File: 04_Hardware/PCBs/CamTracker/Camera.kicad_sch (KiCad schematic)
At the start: 35 parts, among them J10 1.25x15P, J11 22-28-4034, J12 22-28-4034, J9 1.25x15P, U1 SC206EEMDA-G51-UGNDA

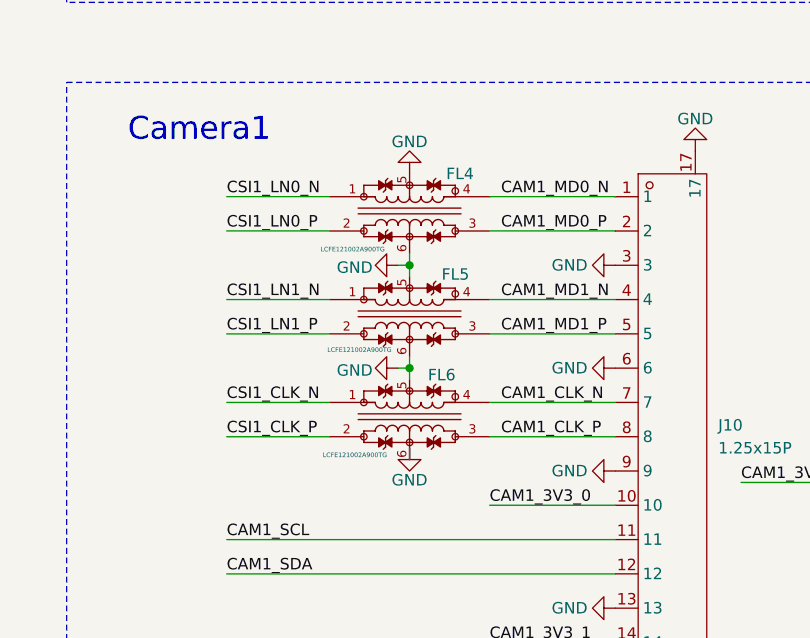
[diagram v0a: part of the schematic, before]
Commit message: feat: Completed Placement v1 in Layout
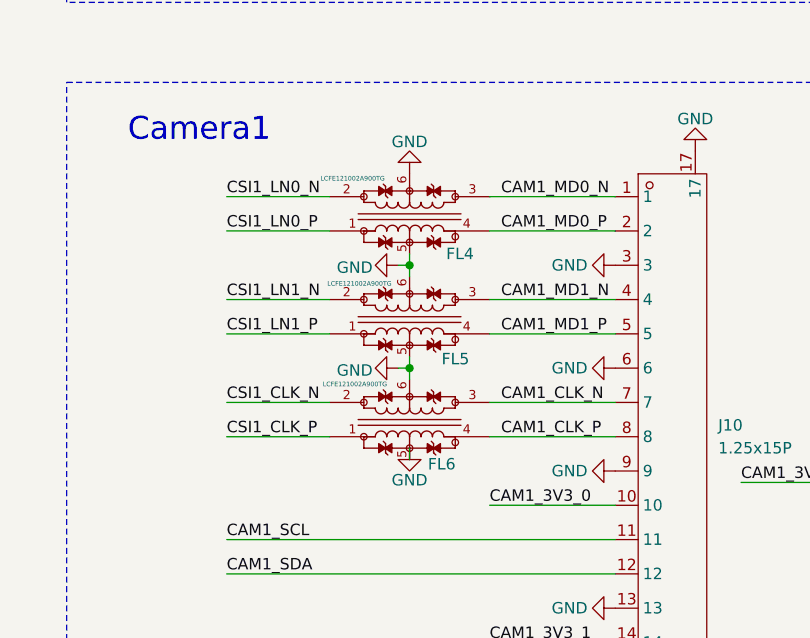
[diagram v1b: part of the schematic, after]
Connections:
- net CAM1_CLK_N: now also FL6.3; no longer FL6.4
- net CAM1_CLK_P: now also FL6.4; no longer FL6.3
- net CAM1_MD0_N: now also FL4.3; no longer FL4.4
- net CAM1_MD0_P: now also FL4.4; no longer FL4.3
- net CAM1_MD1_N: now also FL5.3; no longer FL5.4
- net CAM1_MD1_P: now also FL5.4; no longer FL5.3
- net CSI1_CLK_N: now also FL6.2; no longer FL6.1
- net CSI1_CLK_P: now also FL6.1; no longer FL6.2
- net CSI1_LN0_N: now also FL4.2; no longer FL4.1
- net CSI1_LN0_P: now also FL4.1; no longer FL4.2
- net CSI1_LN1_N: now also FL5.2; no longer FL5.1
- net CSI1_LN1_P: now also FL5.1; no longer FL5.2
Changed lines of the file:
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@@
 	(wire
 		(pts
+			(xy 195.58 152.4) (xy 195.58 151.13)
+		)
+		(stroke
+			(width 0)
+			(type default)
+		)
+	)
+	(wire
+		(pts
 			(xy 195.58 162.56) (xy 194.31 162.56)
 		)
@@
 	(wire
 		(pts
-			(xy 195.58 171.45) (xy 195.58 172.72)
+			(xy 195.58 161.29) (xy 195.58 162.56)
 		)
 		(stroke
@@
 	(wire
 		(pts
-			(xy 175.26 67.31) (xy 186.69 67.31)
+			(xy 195.58 171.45) (xy 195.58 172.72)
 		)
 		(stroke
@@
 	(wire
 		(pts
-			(xy 100.33 118.11) (xy 81.28 118.11)
+			(xy 175.26 67.31) (xy 186.69 67.31)
 		)
 		(stroke
@@
 	(wire
 		(pts
-			(xy 175.26 52.07) (xy 186.69 52.07)
+			(xy 100.33 118.11) (xy 81.28 118.11)
 		)
 		(stroke
@@
 	(wire
 		(pts
-			(xy 274.32 72.39) (xy 274.32 71.12)
+			(xy 175.26 52.07) (xy 186.69 52.07)
 		)
 		(stroke
@@
 	(wire
 		(pts
-			(xy 294.64 175.26) (xy 290.83 175.26)
+			(xy 274.32 72.39) (xy 274.32 71.12)
 		)
 		(stroke
@@
 	(wire
 		(pts
-			(xy 195.58 151.13) (xy 195.58 152.4)
+			(xy 294.64 175.26) (xy 290.83 175.26)
 		)
 		(stroke
@@
 	(wire
 		(pts
+			(xy 195.58 58.42) (xy 195.58 59.69)
+		)
+		(stroke
+			(width 0)
+			(type default)
+		)
+	)
+	(wire
+		(pts
 			(xy 252.73 212.09) (xy 252.73 210.82)
 		)
@@
 	(wire
 		(pts
-			(xy 195.58 149.86) (xy 195.58 151.13)
-		)
-		(stroke
-			(width 0)
-			(type default)
-		)
-	)
-	(wire
-		(pts
 			(xy 201.93 214.63) (xy 213.36 214.63)
 		)
@@
 	(wire
 		(pts
-			(xy 270.51 72.39) (xy 274.32 72.39)
+			(xy 195.58 149.86) (xy 195.58 151.13)
 		)
 		(stroke
@@
 	(wire
 		(pts
-			(xy 175.26 166.37) (xy 186.69 166.37)
+			(xy 270.51 72.39) (xy 274.32 72.39)
 		)
 		(stroke
@@
 	(wire
 		(pts
-			(xy 100.33 76.2) (xy 81.28 76.2)
+			(xy 175.26 166.37) (xy 186.69 166.37)
 		)
 		(stroke
@@
 	(wire
 		(pts
-			(xy 81.28 185.42) (xy 100.33 185.42)
+			(xy 100.33 76.2) (xy 81.28 76.2)
 		)
 		(stroke
@@
 	(wire
 		(pts
-			(xy 195.58 151.13) (xy 194.31 151.13)
+			(xy 81.28 185.42) (xy 100.33 185.42)
 		)
 		(stroke
@@
 	(wire
 		(pts
-			(xy 100.33 106.68) (xy 81.28 106.68)
+			(xy 195.58 151.13) (xy 194.31 151.13)
 		)
 		(stroke
@@
 	(wire
 		(pts
-			(xy 195.58 161.29) (xy 195.58 162.56)
+			(xy 100.33 106.68) (xy 81.28 106.68)
 		)
 		(stroke
@@
 	(wire
 		(pts
-			(xy 195.58 60.96) (xy 195.58 59.69)
-		)
-		(stroke
-			(width 0)
-			(type default)
-		)
-	)
-	(wire
-		(pts
 			(xy 81.28 189.23) (xy 100.33 189.23)
 		)
@@
 	(wire
 		(pts
-			(xy 195.58 58.42) (xy 195.58 59.69)
-		)
-		(stroke
-			(width 0)
-			(type default)
-		)
-	)
-	(wire
-		(pts
 			(xy 292.1 162.56) (xy 276.86 162.56)
 		)
@@
 	(wire
 		(pts
+			(xy 195.58 60.96) (xy 195.58 59.69)
+		)
+		(stroke
+			(width 0)
+			(type default)
+		)
+	)
+	(wire
+		(pts
 			(xy 195.58 163.83) (xy 195.58 162.56)
 		)
@@
 	(symbol
 		(lib_id "000MCLib:LCFE121002A900TG")
-		(at 195.58 146.05 0)
-		(mirror x)
+		(at 195.58 144.78 0)
 		(unit 1)
 		(exclude_from_sim no)
@@
 		(dnp no)
 		(property "Reference" "FL4"
-			(at 199.644 140.97 0)
+			(at 199.644 149.86 0)
 			(effects
 				(font
@@
 		)
 		(property "Value" "LCFE121002A900TG"
-			(at 185.674 149.352 0)
+			(at 185.674 141.478 0)
 			(effects
 				(font
@@
 		)
 		(property "Footprint" "000MCLib:LCFE121002A900TG"
-			(at 222.25 68.91 0)
+			(at 222.25 221.92 0)
 			(effects
 				(font
@@
 		)
 		(property "Datasheet" "https://www.littelfuse.com/~/media/electronics/datasheets/emc_components/littelfuse_emi_filter_lcfe_datasheet.pdf.pdf"
-			(at 222.25 -31.09 0)
+			(at 222.25 321.92 0)
 			(effects
 				(font
@@
 		)
 		(property "Description" "Common Mode Chokes / Filters 90ohms 25% 100A 2 Lines 1210"
-			(at 195.58 144.78 0)
+			(at 195.58 146.05 0)
 			(effects
 				(font
@@
 		)
 		(property "Manufacturer" "LITTELFUSE"
-			(at 222.25 -531.09 0)
+			(at 222.25 821.92 0)
 			(effects
 				(font
@@
 		)
 		(property "Part Number" "LCFE121002A900TG"
-			(at 222.25 -631.09 0)
+			(at 222.25 921.92 0)
 			(effects
 				(font
@@
 	(symbol
 		(lib_id "000MCLib:LCFE121002A900TG")
-		(at 195.58 157.48 0)
-		(mirror x)
+		(at 195.58 156.21 0)
 		(unit 1)
 		(exclude_from_sim no)
@@
 		(dnp no)
 		(property "Reference" "FL5"
-			(at 199.136 152.146 0)
+			(at 199.136 161.544 0)
 			(effects
 				(font
@@
 		)
 		(property "Value" "LCFE121002A900TG"
-			(at 186.436 160.528 0)
+			(at 186.436 153.162 0)
 			(effects
 				(font
@@
 		)
 		(property "Footprint" "000MCLib:LCFE121002A900TG"
-			(at 222.25 80.34 0)
+			(at 222.25 233.35 0)
 			(effects
 				(font
@@
 		)
 		(property "Datasheet" "https://www.littelfuse.com/~/media/electronics/datasheets/emc_components/littelfuse_emi_filter_lcfe_datasheet.pdf.pdf"
-			(at 222.25 -19.66 0)
+			(at 222.25 333.35 0)
 			(effects
 				(font
@@
 		)
 		(property "Description" "Common Mode Chokes / Filters 90ohms 25% 100A 2 Lines 1210"
-			(at 195.58 156.21 0)
+			(at 195.58 157.48 0)
 			(effects
 				(font
@@
 		)
 		(property "Manufacturer" "LITTELFUSE"
-			(at 222.25 -519.66 0)
+			(at 222.25 833.35 0)
 			(effects
 				(font
@@
 		)
 		(property "Part Number" "LCFE121002A900TG"
-			(at 222.25 -619.66 0)
+			(at 222.25 933.35 0)
 			(effects
 				(font
@@
 	(symbol
 		(lib_id "000MCLib:LCFE121002A900TG")
-		(at 195.58 168.91 0)
-		(mirror x)
+		(at 195.58 167.64 0)
 		(unit 1)
 		(exclude_from_sim no)
@@
 		(dnp no)
 		(property "Reference" "FL6"
-			(at 197.612 163.322 0)
+			(at 197.612 173.228 0)
 			(effects
 				(font
@@
 		)
 		(property "Value" "LCFE121002A900TG"
-			(at 185.928 172.212 0)
+			(at 185.928 164.338 0)
 			(effects
 				(font
@@
 		)
 		(property "Footprint" "000MCLib:LCFE121002A900TG"
-			(at 222.25 91.77 0)
+			(at 222.25 244.78 0)
 			(effects
 				(font
@@
 		)
 		(property "Datasheet" "https://www.littelfuse.com/~/media/electronics/datasheets/emc_components/littelfuse_emi_filter_lcfe_datasheet.pdf.pdf"
-			(at 222.25 -8.23 0)
+			(at 222.25 344.78 0)
 			(effects
 				(font
@@
 		)
 		(property "Description" "Common Mode Chokes / Filters 90ohms 25% 100A 2 Lines 1210"
-			(at 195.58 167.64 0)
+			(at 195.58 168.91 0)
 			(effects
 				(font
@@
 		)
 		(property "Manufacturer" "LITTELFUSE"
-			(at 222.25 -508.23 0)
+			(at 222.25 844.78 0)
 			(effects
 				(font
@@
 		)
 		(property "Part Number" "LCFE121002A900TG"
-			(at 222.25 -608.23 0)
+			(at 222.25 944.78 0)
 			(effects
 				(font

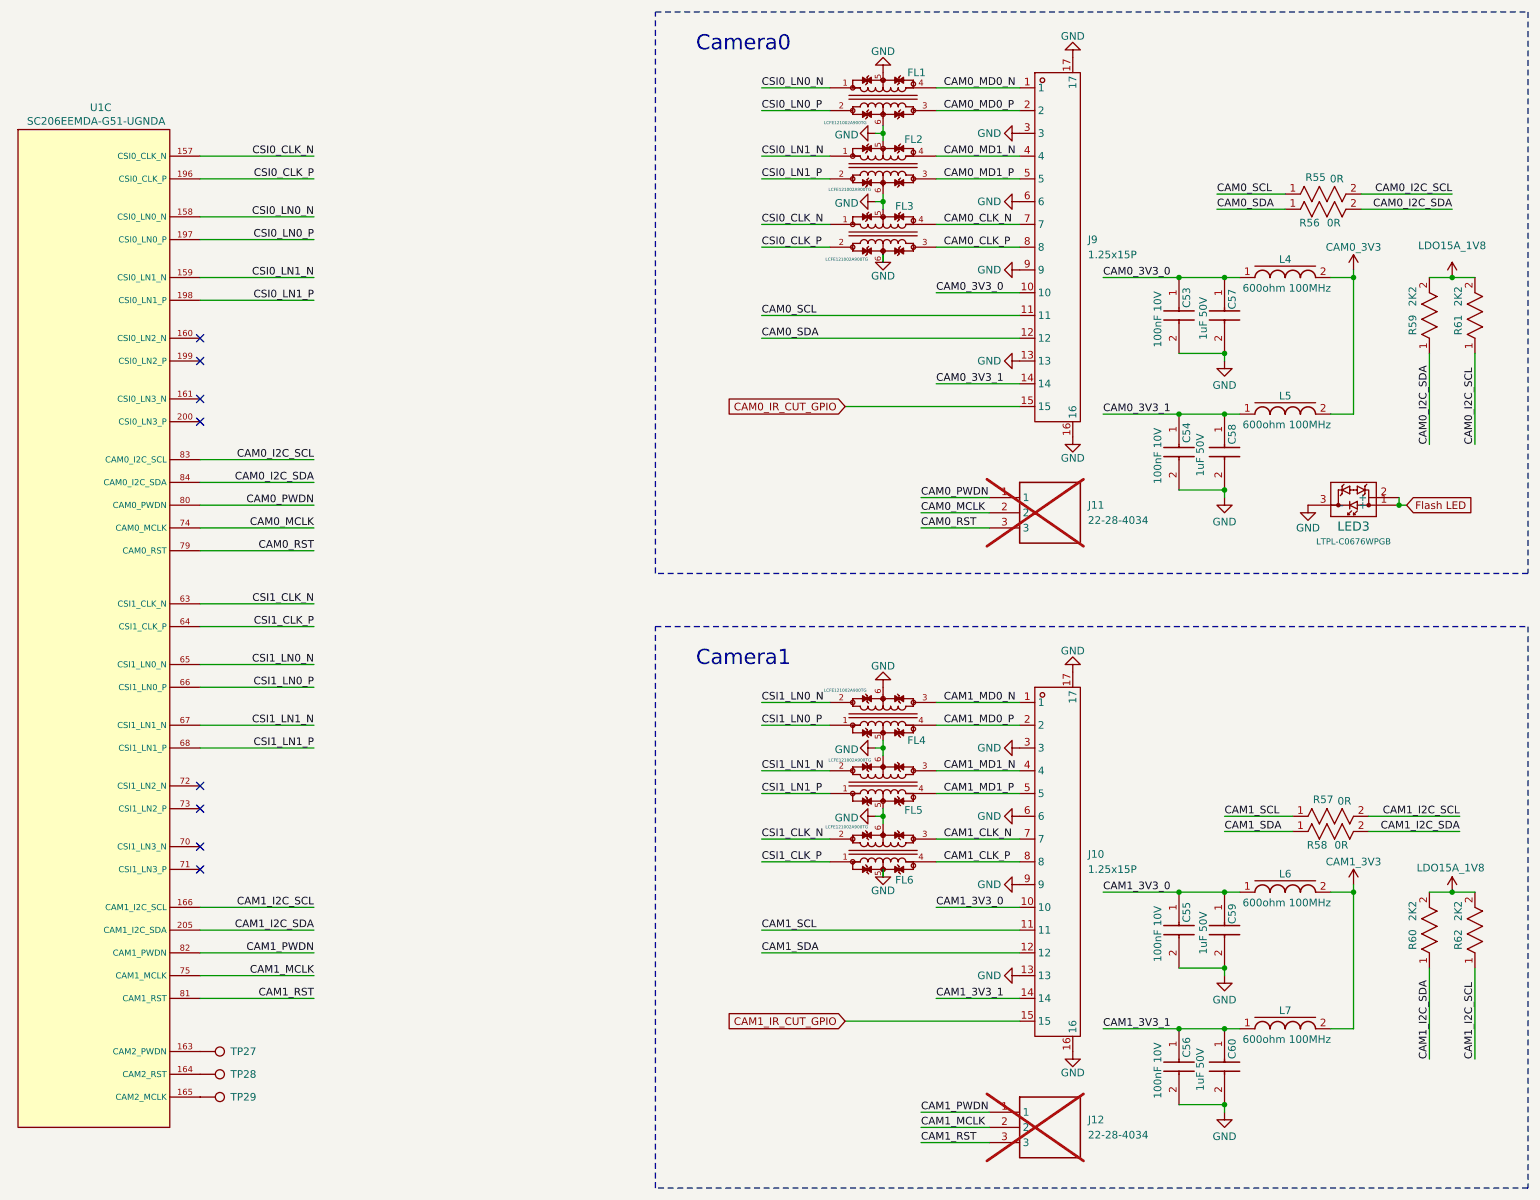
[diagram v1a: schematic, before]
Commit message: feat(layout): Completed Layout Design with new Camera Connectors
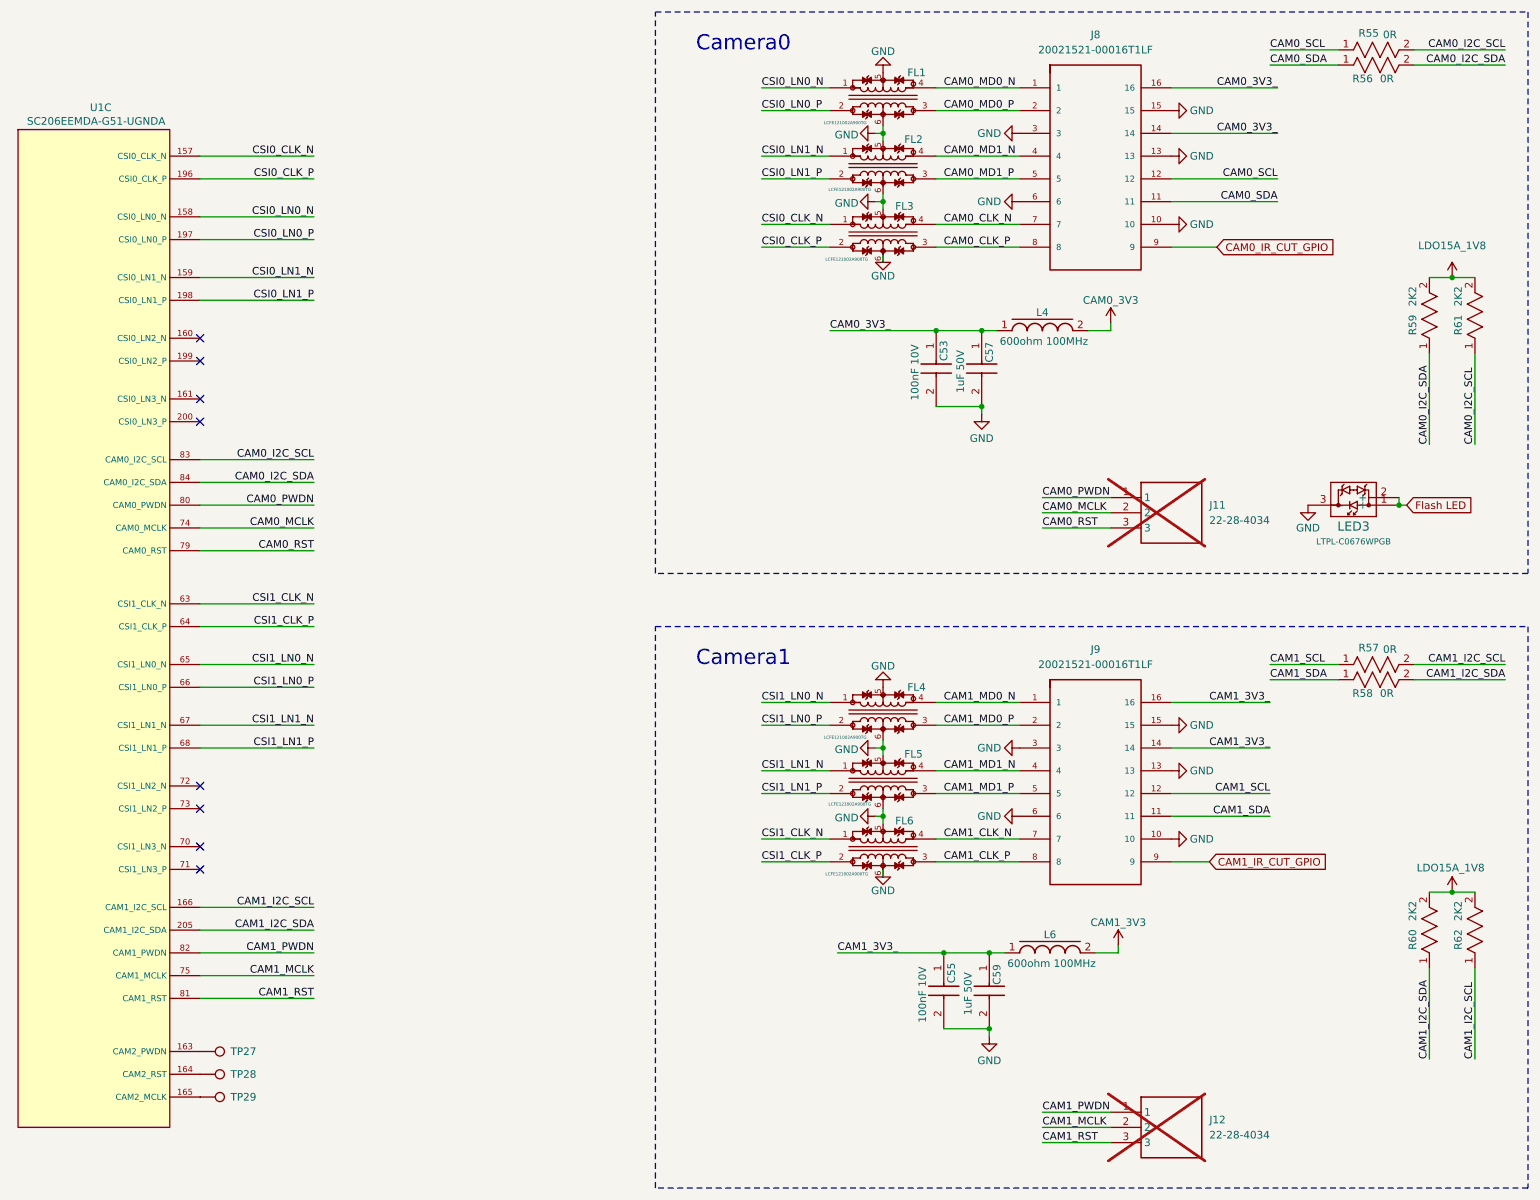
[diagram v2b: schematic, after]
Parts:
- removed C54, C56: 100nF 10V, 000MCLib:CAPC1005X55N, symbol 000MCLib:GRM155R71A104KA01D
- removed C58, C60: 1uF 50V, 000MCLib:CAPC1005X55N, symbol 000MCLib:GRM155R61H105KE05D
- removed J10, J9: 1.25x15P, 000MCLib:CONN-SMD_15P-P1.25_HCTL_HC-1.25-15PLT, symbol 000MCLib:1.25-15P LT
- removed L5, L7: 600ohm 100MHz, 000MCLib:0402, symbol 000MCLib:7427927291
- added J8, J9: 20021521-00016T1LF, 000MCLib:AMPHENOL_20021521-00016T1LF, symbol 000MCLib:20021521-00016T1LF
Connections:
- net CAM0_CLK_N: now also J8.7
- net CAM0_CLK_P: now also J8.8
- net CAM0_IR_CUT_GPIO: now also J8.9
- net CAM0_MD0_N: now also J8.1
- net CAM0_MD0_P: now also J8.2
- net CAM0_MD1_N: now also J8.4
- net CAM0_MD1_P: now also J8.5
- net CAM0_SCL: now also J8.12
- net CAM0_SDA: now also J8.11
- net CAM1_CLK_N: now also FL6.4, J9.7; no longer FL6.3
- net CAM1_CLK_P: now also FL6.3, J9.8; no longer FL6.4
- net CAM1_IR_CUT_GPIO: now also J9.9
- net CAM1_MD0_N: now also FL4.4, J9.1; no longer FL4.3
- net CAM1_MD0_P: now also FL4.3, J9.2; no longer FL4.4
- net CAM1_MD1_N: now also FL5.4, J9.4; no longer FL5.3
- net CAM1_MD1_P: now also FL5.3, J9.5; no longer FL5.4
- net CAM1_SCL: now also J9.12
- net CAM1_SDA: now also J9.11
- net CSI1_CLK_N: now also FL6.1; no longer FL6.2
- net CSI1_CLK_P: now also FL6.2; no longer FL6.1
- net CSI1_LN0_N: now also FL4.1; no longer FL4.2
- net CSI1_LN0_P: now also FL4.2; no longer FL4.1
- net CSI1_LN1_N: now also FL5.1; no longer FL5.2
- net CSI1_LN1_P: now also FL5.2; no longer FL5.1
- net GND: now also J8.10, J8.13, J8.15, J8.3, J8.6, J9.10, J9.13, J9.15, J9.3, J9.6
- net CAM0_3V3_0 renamed CAM0_3V3_
- net CAM0_3V3_: now also J8.14, J8.16
- net CAM1_3V3_0 renamed CAM1_3V3_
- net CAM1_3V3_: now also J9.14, J9.16
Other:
- moved on the sheet: C53, C55, C57, C59, J11, J12, L4, L6, R55, R56, R57, R58
